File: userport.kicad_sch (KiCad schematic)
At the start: 49 parts, among them J3 C64_User_Port, J4 Mini-DIN-8-With-Shield, J5 C64_Tape_Port, J6 OKR-T/3-W12-C, U1 74LS595, U10 74LS125, U11 74LS595, U2 74LVC165, U3 74LS125, U4 74LS595, U5 74LVC165, U6 74LS595, U7 74LVC165, U8 74LS125, U9 74LS125

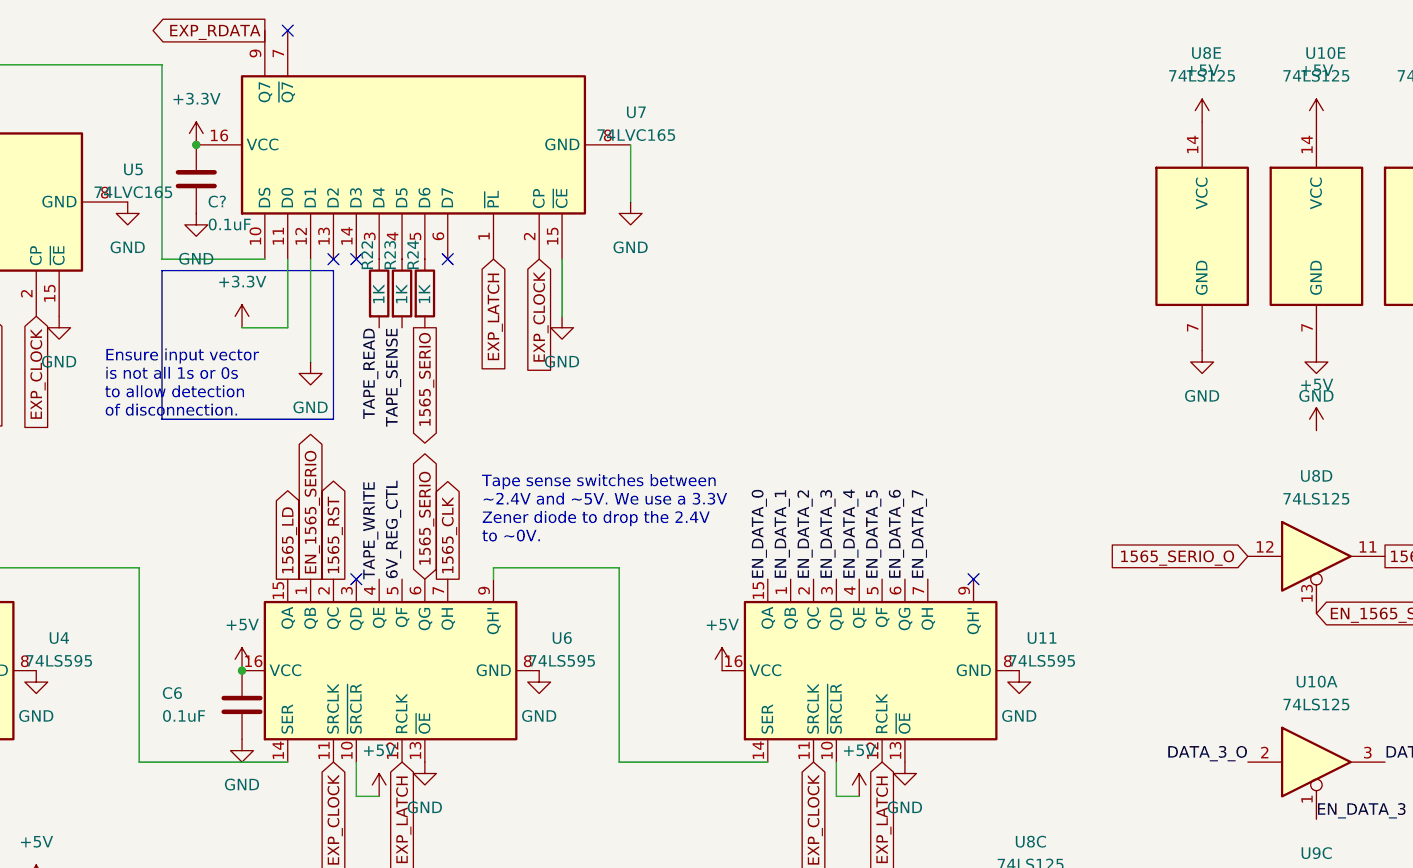
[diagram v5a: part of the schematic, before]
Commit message: add U8 decoupling cap
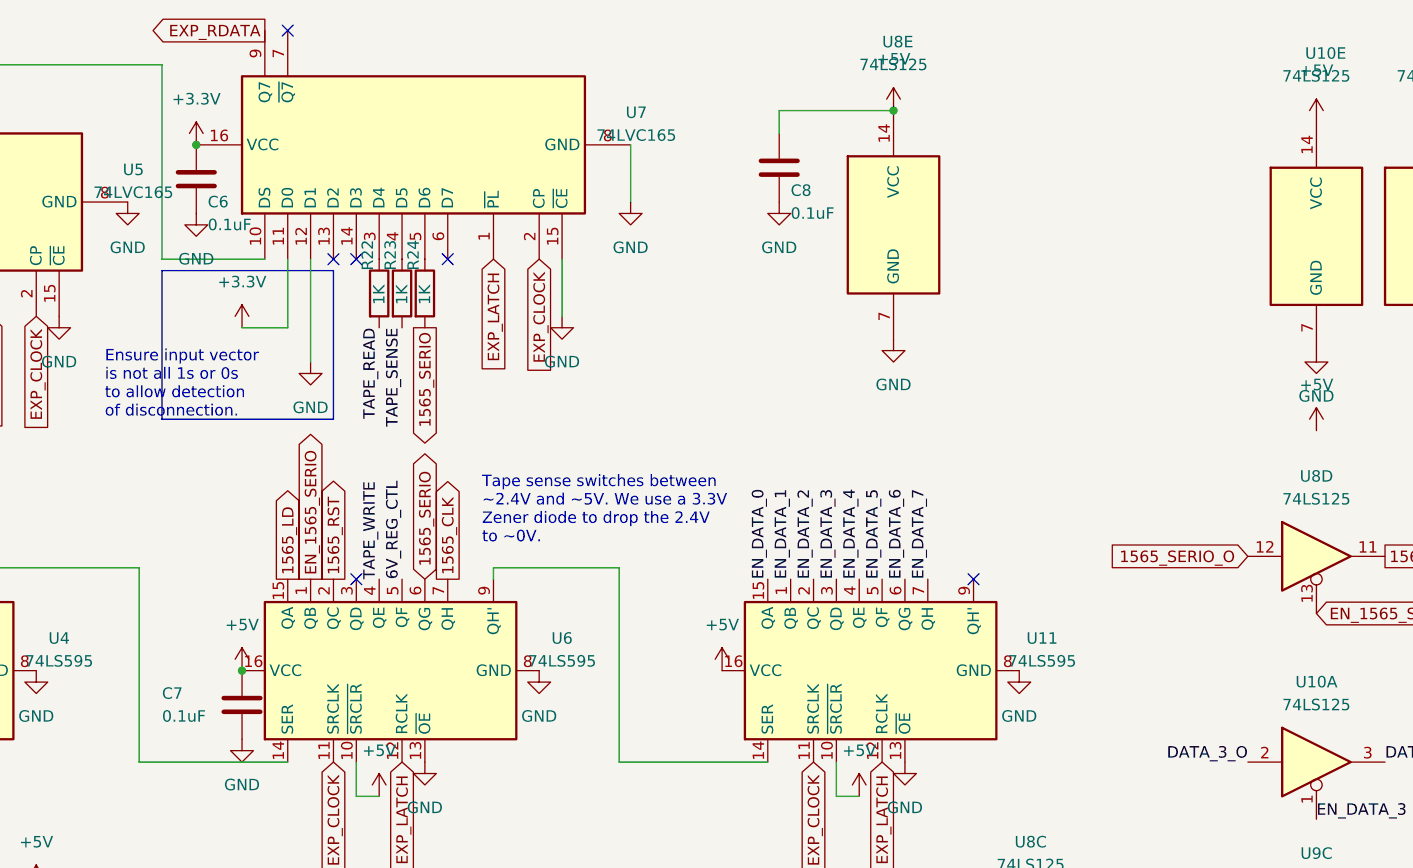
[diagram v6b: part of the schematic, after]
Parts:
- added C8: 0.1uF, Capacitor_THT:C_Disc_D5.0mm_W2.5mm_P5.00mm, symbol Device:C
- gave numbers to parts that had none: 1
- renumbered C6 to C7
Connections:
- net +5V: now also C8.1
- net GND: now also C8.2
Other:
- moved on the sheet: U8E

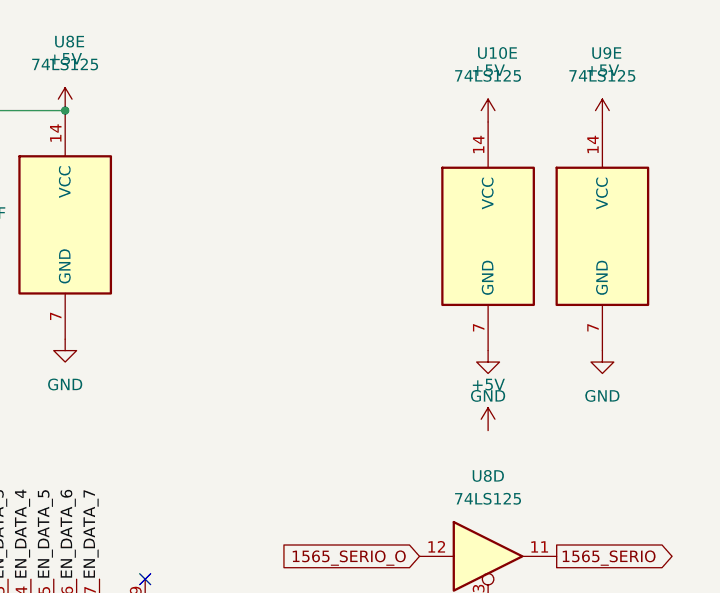
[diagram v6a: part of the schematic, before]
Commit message: add U9 U10 decoupling caps
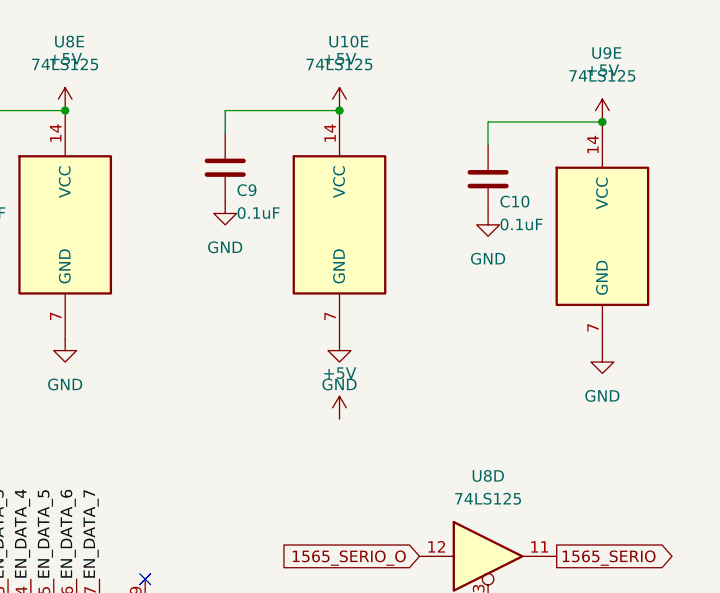
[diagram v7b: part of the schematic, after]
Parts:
- added C10, C9: 0.1uF, Capacitor_THT:C_Disc_D5.0mm_W2.5mm_P5.00mm, symbol Device:C
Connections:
- net +5V: now also C10.1, C9.1
- net GND: now also C10.2, C9.2
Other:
- moved on the sheet: U10E
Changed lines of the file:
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@@
 (kicad_sch (version 20211123) (generator eeschema)
   (paper "A4")
+  (junction (at 242.57 22.86) (diameter 0) (color 0 0 0 0)
+  )
   (junction (at 161.29 180.34) (diameter 0) (color 0 0 0 0)
   )
@@
   (junction (at 161.29 193.04) (diameter 0) (color 0 0 0 0)
   )
+  (junction (at 271.78 24.13) (diameter 0) (color 0 0 0 0)
+  )
   (junction (at 31.115 135.89) (diameter 0) (color 0 0 0 0)
   )
@@
     (stroke (width 0) (type default) (color 0 0 0 0))
   )
+  (wire (pts (xy 259.08 26.67) (xy 259.08 24.13))
+    (stroke (width 0) (type default) (color 0 0 0 0))
+  )
   (wire (pts (xy 31.115 123.19) (xy 31.115 135.89))
     (stroke (width 0) (type default) (color 0 0 0 0))
@@
     (stroke (width 0) (type default) (color 0 0 0 0))
   )
+  (wire (pts (xy 229.87 25.4) (xy 229.87 22.86))
+    (stroke (width 0) (type default) (color 0 0 0 0))
+  )
   (wire (pts (xy 134.62 185.42) (xy 148.59 185.42))
     (stroke (width 0) (type default) (color 0 0 0 0))
@@
     (stroke (width 0) (type default) (color 0 0 0 0))
   )
+  (wire (pts (xy 259.08 24.13) (xy 271.78 24.13))
+    (stroke (width 0) (type default) (color 0 0 0 0))
+  )
   (wire (pts (xy 62.23 175.26) (xy 69.85 175.26))
     (stroke (width 0) (type default) (color 0 0 0 0))
@@
     (stroke (width 0) (type default) (color 0 0 0 0))
   )
+  (wire (pts (xy 229.87 22.86) (xy 242.57 22.86))
+    (stroke (width 0) (type default) (color 0 0 0 0))
+  )
   (wire (pts (xy 62.23 177.8) (xy 69.85 177.8))
     (stroke (width 0) (type default) (color 0 0 0 0))
@@
     (pin "1")
   )
+  (symbol (lib_id "power:GND") (at 259.08 34.29 0) (unit 1)
+    (in_bom yes) (on_board yes) (fields_autoplaced)
+    (property "Reference" "#PWR082" (id 0) (at 259.08 40.64 0)
+      (effects (font (size 1.27 1.27)) hide)
+    )
+    (property "Value" "GND" (id 1) (at 259.08 39.37 0))
+    (property "Footprint" "" (id 2) (at 259.08 34.29 0)
+      (effects (font (size 1.27 1.27)) hide)
+    )
+    (property "Datasheet" "" (id 3) (at 259.08 34.29 0)
+      (effects (font (size 1.27 1.27)) hide)
+    )
+    (pin "1")
+  )
   (symbol (lib_id "power:GND") (at 130.81 140.97 0) (unit 1)
     (in_bom yes) (on_board yes) (fields_autoplaced)
@@
   (symbol (lib_id "power:GND") (at 271.78 49.53 0) (unit 1)
     (in_bom yes) (on_board yes) (fields_autoplaced)
-    (property "Reference" "#PWR082" (id 0) (at 271.78 55.88 0)
+    (property "Reference" "#PWR084" (id 0) (at 271.78 55.88 0)
       (effects (font (size 1.27 1.27)) hide)
     )
@@
     (pin "1")
   )
+  (symbol (lib_id "Device:C") (at 259.08 30.48 0) (unit 1)
+    (in_bom yes) (on_board yes)
+    (property "Reference" "C10" (id 0) (at 260.35 33.02 0)
+      (effects (font (size 1.27 1.27)) (justify left))
+    )
+    (property "Value" "0.1uF" (id 1) (at 260.35 35.56 0)
+      (effects (font (size 1.27 1.27)) (justify left))
+    )
+    (property "Footprint" "Capacitor_THT:C_Disc_D5.0mm_W2.5mm_P5.00mm" (id 2) (at 260.0452 34.29 0)
+      (effects (font (size 1.27 1.27)) hide)
+    )
+    (property "Datasheet" "~" (id 3) (at 259.08 30.48 0)
+      (effects (font (size 1.27 1.27)) hide)
+    )
+    (pin "1")
+    (pin "2")
+  )
   (symbol (lib_id "power:GND") (at 62.23 187.96 0) (unit 1)
     (in_bom yes) (on_board yes) (fields_autoplaced)
@@
     (pin "9")
   )
+  (symbol (lib_id "power:GND") (at 229.87 33.02 0) (unit 1)
+    (in_bom yes) (on_board yes) (fields_autoplaced)
+    (property "Reference" "#PWR078" (id 0) (at 229.87 39.37 0)
+      (effects (font (size 1.27 1.27)) hide)
+    )
+    (property "Value" "GND" (id 1) (at 229.87 38.1 0))
+    (property "Footprint" "" (id 2) (at 229.87 33.02 0)
+      (effects (font (size 1.27 1.27)) hide)
+    )
+    (property "Datasheet" "" (id 3) (at 229.87 33.02 0)
+      (effects (font (size 1.27 1.27)) hide)
+    )
+    (pin "1")
+  )
   (symbol (lib_id "power:GND") (at 199.39 33.02 0) (unit 1)
     (in_bom yes) (on_board yes) (fields_autoplaced)
@@
     (pin "6")
   )
+  (symbol (lib_id "Device:C") (at 229.87 29.21 0) (unit 1)
+    (in_bom yes) (on_board yes)
+    (property "Reference" "C9" (id 0) (at 231.14 31.75 0)
+      (effects (font (size 1.27 1.27)) (justify left))
+    )
+    (property "Value" "0.1uF" (id 1) (at 231.14 34.29 0)
+      (effects (font (size 1.27 1.27)) (justify left))
+    )
+    (property "Footprint" "Capacitor_THT:C_Disc_D5.0mm_W2.5mm_P5.00mm" (id 2) (at 230.8352 33.02 0)
+      (effects (font (size 1.27 1.27)) hide)
+    )
+    (property "Datasheet" "~" (id 3) (at 229.87 29.21 0)
+      (effects (font (size 1.27 1.27)) hide)
+    )
+    (pin "1")
+    (pin "2")
+  )
   (symbol (lib_id "power:GND") (at 119.38 45.72 0) (unit 1)
     (in_bom yes) (on_board yes) (fields_autoplaced)
@@
     (pin "1")
   )
-  (symbol (lib_id "power:+5V") (at 259.08 24.13 0) (unit 1)
+  (symbol (lib_id "power:+5V") (at 242.57 22.86 0) (unit 1)
     (in_bom yes) (on_board yes) (fields_autoplaced)
-    (property "Reference" "#PWR078" (id 0) (at 259.08 27.94 0)
+    (property "Reference" "#PWR079" (id 0) (at 242.57 26.67 0)
       (effects (font (size 1.27 1.27)) hide)
     )
-    (property "Value" "+5V" (id 1) (at 259.08 18.415 0))
-    (property "Footprint" "" (id 2) (at 259.08 24.13 0)
+    (property "Value" "+5V" (id 1) (at 242.57 17.145 0))
+    (property "Footprint" "" (id 2) (at 242.57 22.86 0)
       (effects (font (size 1.27 1.27)) hide)
     )
-    (property "Datasheet" "" (id 3) (at 259.08 24.13 0)
+    (property "Datasheet" "" (id 3) (at 242.57 22.86 0)
       (effects (font (size 1.27 1.27)) hide)
     )
@@
   (symbol (lib_id "power:+5V") (at 271.78 24.13 0) (unit 1)
     (in_bom yes) (on_board yes) (fields_autoplaced)
-    (property "Reference" "#PWR081" (id 0) (at 271.78 27.94 0)
+    (property "Reference" "#PWR083" (id 0) (at 271.78 27.94 0)
       (effects (font (size 1.27 1.27)) hide)
     )
@@
     (pin "1")
   )
-  (symbol (lib_id "power:+5V") (at 259.08 58.42 0) (unit 1)
+  (symbol (lib_id "power:+5V") (at 242.57 57.15 0) (unit 1)
     (in_bom yes) (on_board yes) (fields_autoplaced)
-    (property "Reference" "#PWR080" (id 0) (at 259.08 62.23 0)
+    (property "Reference" "#PWR081" (id 0) (at 242.57 60.96 0)
       (effects (font (size 1.27 1.27)) hide)
     )
-    (property "Value" "+5V" (id 1) (at 259.08 53.34 0))
-    (property "Footprint" "" (id 2) (at 259.08 58.42 0)
+    (property "Value" "+5V" (id 1) (at 242.57 52.07 0))
+    (property "Footprint" "" (id 2) (at 242.57 57.15 0)
       (effects (font (size 1.27 1.27)) hide)
     )
-    (property "Datasheet" "" (id 3) (at 259.08 58.42 0)
+    (property "Datasheet" "" (id 3) (at 242.57 57.15 0)
       (effects (font (size 1.27 1.27)) hide)
     )
@@
     (pin "9")
   )
-  (symbol (lib_id "74xx:74LS125") (at 259.08 36.83 0) (unit 5)
+  (symbol (lib_id "74xx:74LS125") (at 242.57 35.56 0) (unit 5)
     (in_bom yes) (on_board yes)
-    (property "Reference" "U10" (id 0) (at 257.81 16.51 0)
+    (property "Reference" "U10" (id 0) (at 241.3 15.24 0)
       (effects (font (size 1.27 1.27)) (justify left))
     )
-    (property "Value" "74LS125" (id 1) (at 255.27 19.05 0)
+    (property "Value" "74LS125" (id 1) (at 238.76 17.78 0)
       (effects (font (size 1.27 1.27)) (justify left))
     )
-    (property "Footprint" "snapeda:DIP-14_74LS06" (id 2) (at 259.08 36.83 0)
+    (property "Footprint" "snapeda:DIP-14_74LS06" (id 2) (at 242.57 35.56 0)
       (effects (font (size 1.27 1.27)) hide)
     )
-    (property "Datasheet" "http://www.ti.com/lit/gpn/sn74LS125" (id 3) (at 259.08 36.83 0)
+    (property "Datasheet" "http://www.ti.com/lit/gpn/sn74LS125" (id 3) (at 242.57 35.56 0)
       (effects (font (size 1.27 1.27)) hide)
     )
@@
     (pin "2")
   )
-  (symbol (lib_id "power:GND") (at 259.08 49.53 0) (unit 1)
+  (symbol (lib_id "power:GND") (at 242.57 48.26 0) (unit 1)
     (in_bom yes) (on_board yes) (fields_autoplaced)
-    (property "Reference" "#PWR079" (id 0) (at 259.08 55.88 0)
+    (property "Reference" "#PWR080" (id 0) (at 242.57 54.61 0)
       (effects (font (size 1.27 1.27)) hide)
     )
-    (property "Value" "GND" (id 1) (at 259.08 54.61 0))
-    (property "Footprint" "" (id 2) (at 259.08 49.53 0)
+    (property "Value" "GND" (id 1) (at 242.57 53.34 0))
+    (property "Footprint" "" (id 2) (at 242.57 48.26 0)
       (effects (font (size 1.27 1.27)) hide)
     )
-    (property "Datasheet" "" (id 3) (at 259.08 49.53 0)
+    (property "Datasheet" "" (id 3) (at 242.57 48.26 0)
       (effects (font (size 1.27 1.27)) hide)
     )

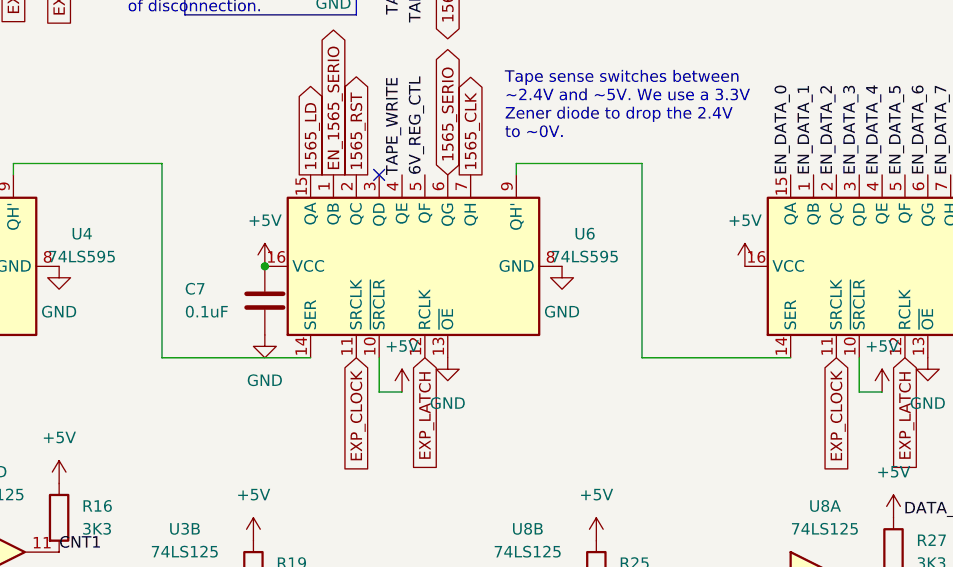
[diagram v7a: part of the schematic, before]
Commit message: add U11 decoupling cap
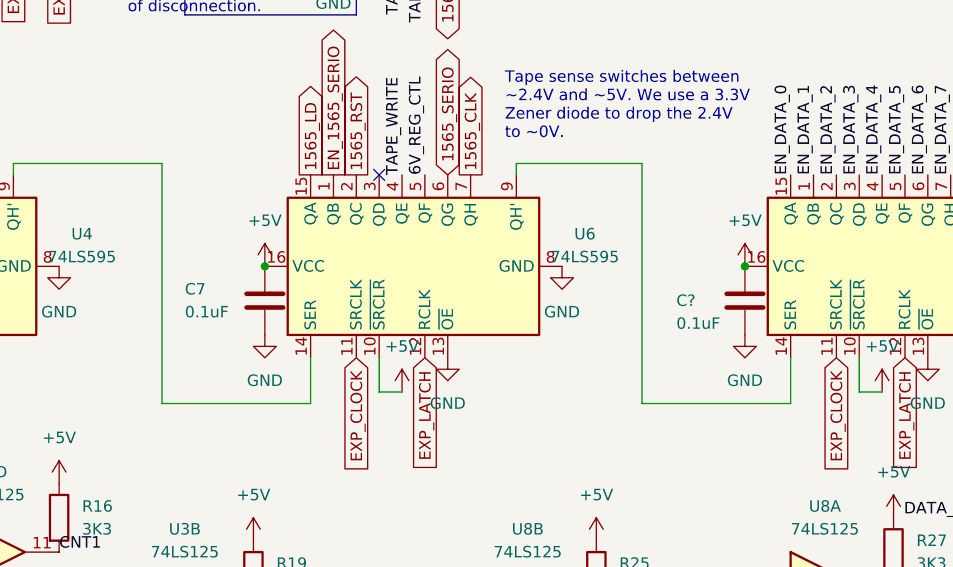
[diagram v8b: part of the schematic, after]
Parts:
- added C?: 0.1uF, Capacitor_THT:C_Disc_D5.0mm_W2.5mm_P5.00mm, symbol Device:C
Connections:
- net +5V: now also C?.1
- net GND: now also C?.2
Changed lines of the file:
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@@
   (junction (at 148.59 193.04) (diameter 0) (color 0 0 0 0)
   )
+  (junction (at 193.04 85.09) (diameter 0) (color 0 0 0 0)
+  )
   (junction (at 27.94 85.09) (diameter 0) (color 0 0 0 0)
   )
@@
     (stroke (width 0) (type default) (color 0 0 0 0))
   )
-  (wire (pts (xy 181.61 73.66) (xy 181.61 95.25))
+  (wire (pts (xy 181.61 73.66) (xy 181.61 100.33))
     (stroke (width 0) (type default) (color 0 0 0 0))
   )
@@
     (stroke (width 0) (type default) (color 0 0 0 0))
   )
-  (wire (pts (xy 181.61 95.25) (xy 198.12 95.25))
+  (wire (pts (xy 181.61 100.33) (xy 198.12 100.33))
     (stroke (width 0) (type default) (color 0 0 0 0))
   )
@@
     (stroke (width 0) (type default) (color 0 0 0 0))
   )
-  (wire (pts (xy 128.27 73.66) (xy 128.27 95.25))
+  (wire (pts (xy 128.27 73.66) (xy 128.27 100.33))
     (stroke (width 0) (type default) (color 0 0 0 0))
   )
@@
     (stroke (width 0) (type default) (color 0 0 0 0))
   )
-  (wire (pts (xy 128.27 95.25) (xy 144.78 95.25))
+  (wire (pts (xy 128.27 100.33) (xy 144.78 100.33))
     (stroke (width 0) (type default) (color 0 0 0 0))
   )
@@
     (stroke (width 0) (type default) (color 0 0 0 0))
   )
+  (wire (pts (xy 144.78 100.33) (xy 144.78 95.25))
+    (stroke (width 0) (type default) (color 0 0 0 0))
+  )
   (wire (pts (xy 175.26 39.37) (xy 175.26 45.72))
     (stroke (width 0) (type default) (color 0 0 0 0))
@@
     (stroke (width 0) (type default) (color 0 0 0 0))
   )
+  (wire (pts (xy 198.12 100.33) (xy 198.12 95.25))
+    (stroke (width 0) (type default) (color 0 0 0 0))
+  )
   (wire (pts (xy 39.37 177.8) (xy 49.53 177.8))
     (stroke (width 0) (type default) (color 0 0 0 0))
@@
     (pin "1")
   )
+  (symbol (lib_id "power:GND") (at 193.04 92.71 0) (unit 1)
+    (in_bom yes) (on_board yes) (fields_autoplaced)
+    (property "Reference" "#PWR?" (id 0) (at 193.04 99.06 0)
+      (effects (font (size 1.27 1.27)) hide)
+    )
+    (property "Value" "GND" (id 1) (at 193.04 97.79 0))
+    (property "Footprint" "" (id 2) (at 193.04 92.71 0)
+      (effects (font (size 1.27 1.27)) hide)
+    )
+    (property "Datasheet" "" (id 3) (at 193.04 92.71 0)
+      (effects (font (size 1.27 1.27)) hide)
+    )
+    (pin "1")
+  )
   (symbol (lib_id "Device:R") (at 106.68 49.53 0) (unit 1)
     (in_bom yes) (on_board yes)
@@
       (effects (font (size 1.27 1.27)) hide)
     )
+    (pin "1")
+    (pin "2")
+  )
+  (symbol (lib_id "Device:C") (at 193.04 88.9 0) (unit 1)
+    (in_bom yes) (on_board yes)
+    (property "Reference" "C?" (id 0) (at 185.42 88.9 0)
+      (effects (font (size 1.27 1.27)) (justify left))
+    )
+    (property "Value" "0.1uF" (id 1) (at 185.42 91.44 0)
+      (effects (font (size 1.27 1.27)) (justify left))
+    )
+    (property "Footprint" "Capacitor_THT:C_Disc_D5.0mm_W2.5mm_P5.00mm" (id 2) (at 194.0052 92.71 0)
+      (effects (font (size 1.27 1.27)) hide)
+    )
+    (property "Datasheet" "~" (id 3) (at 193.04 88.9 0)
+      (effects (font (size 1.27 1.27)) hide)
+    )
